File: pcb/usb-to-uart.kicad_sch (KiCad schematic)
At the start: 18 parts, among them J10 Conn_01x08_Pin, J13 Conn_01x04_Pin, J5 Conn_01x08_Pin, Q1 UMH3N, U4 CP2102N-Axx-xQFN28

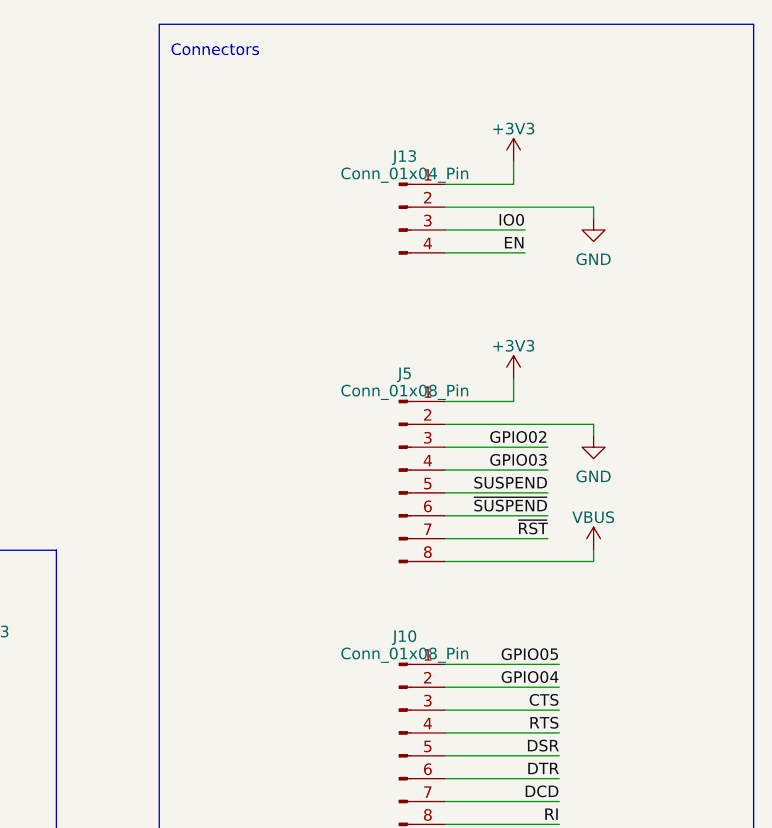
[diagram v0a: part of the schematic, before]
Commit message: Removed unpopulated pin header from BOM
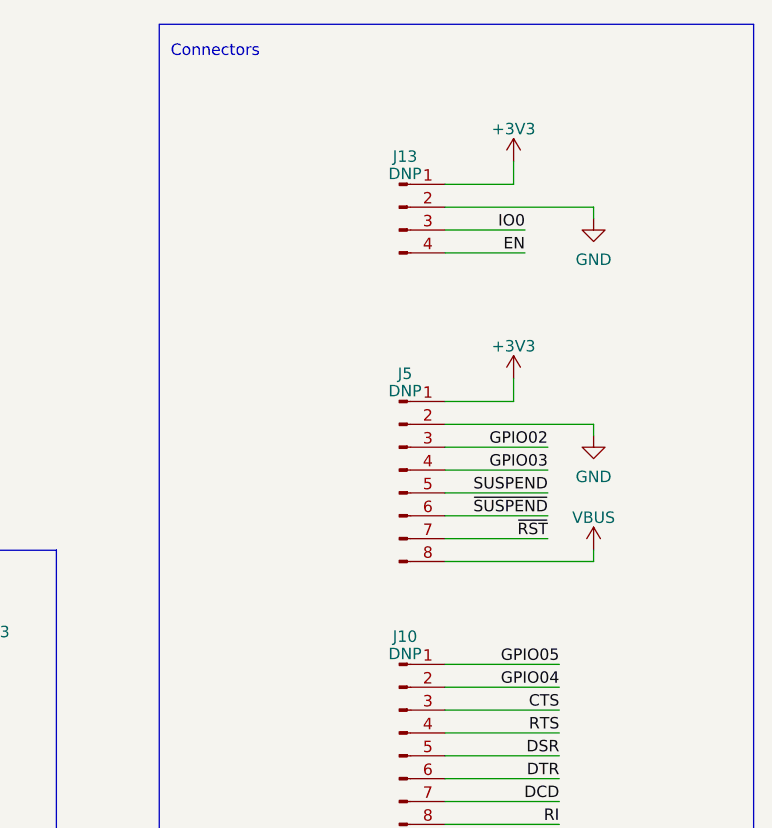
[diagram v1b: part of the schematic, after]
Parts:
- J10, J5: value Conn_01x08_Pin -> DNP; now left out of the parts list
- J13: value Conn_01x04_Pin -> DNP; now left out of the parts list
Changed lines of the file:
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@@
   )
   (symbol (lib_id "Connector:Conn_01x04_Pin") (at 207.01 43.18 0) (unit 1)
-    (in_bom yes) (on_board yes) (dnp no) (fields_autoplaced)
+    (in_bom no) (on_board yes) (dnp no) (fields_autoplaced)
     (property "Reference" "J13" (at 207.645 37.5539 0)
       (effects (font (size 1.27 1.27)))
     )
-    (property "Value" "Conn_01x04_Pin" (at 207.645 39.4749 0)
+    (property "Value" "DNP" (at 207.645 39.4749 0)
       (effects (font (size 1.27 1.27)))
     )
@@
   )
   (symbol (lib_id "Connector:Conn_01x08_Pin") (at 207.01 72.39 0) (unit 1)
-    (in_bom yes) (on_board yes) (dnp no) (fields_autoplaced)
+    (in_bom no) (on_board yes) (dnp no) (fields_autoplaced)
     (property "Reference" "J5" (at 207.645 61.6839 0)
       (effects (font (size 1.27 1.27)))
     )
-    (property "Value" "Conn_01x08_Pin" (at 207.645 63.6049 0)
+    (property "Value" "DNP" (at 207.645 63.6049 0)
       (effects (font (size 1.27 1.27)))
     )
@@
   )
   (symbol (lib_id "Connector:Conn_01x08_Pin") (at 207.01 101.6 0) (unit 1)
-    (in_bom yes) (on_board yes) (dnp no) (fields_autoplaced)
+    (in_bom no) (on_board yes) (dnp no) (fields_autoplaced)
     (property "Reference" "J10" (at 207.645 90.8939 0)
       (effects (font (size 1.27 1.27)))
     )
-    (property "Value" "Conn_01x08_Pin" (at 207.645 92.8149 0)
-      (effects (font (size 1.27 1.27)))
-    )
+    (property "Value" "DNP" (at 207.645 92.8149 0)
+      (effects (font (size 1.27 1.27)))
+    )
